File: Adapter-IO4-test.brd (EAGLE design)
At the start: 22 parts, among them CON1 CONNECTOR-IO4INV

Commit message: simplified design
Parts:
- removed LED5, LED6, LED7, LED8: (no value), SPCoast:LED5MM
- added BOARD1: BOARD50X50-NOHOLES, SPCoast:BOARD-SEEED5X5-NOHOLES
- moved Q1 36.9 mm to (5.71, 41.3), turned to 90 degrees
- moved Q2 36.9 mm to (15.9, 41.3), turned to 90 degrees
- moved Q3 36.9 mm to (26.0, 41.3), turned to 90 degrees
- moved Q4 36.9 mm to (36.2, 41.3), turned to 90 degrees
- moved LED1 29.2 mm to (10.8, 37.5)
- moved LED2 29.2 mm to (21.0, 37.5)
- moved LED3 29.2 mm to (31.1, 37.5)
- moved LED4 29.2 mm to (41.3, 37.5)
- moved R1 29.2 mm to (5.71, 37.5)
- moved R2 29.2 mm to (15.9, 37.5)
- moved R3 29.2 mm to (26.0, 37.5)
- moved R4 29.2 mm to (36.2, 37.5)
- moved SW1 5.24 mm to (10.8, 29.8)
- moved SW2 5.24 mm to (21.0, 29.8)
- moved SW3 5.24 mm to (31.1, 29.8)
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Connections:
- net GND: no longer LED5.K, LED6.K, LED7.K, LED8.K
- net N$16: no longer LED8.A
- net N$2: no longer LED5.A
- net N$4: no longer LED6.A
- net N$6: no longer LED7.A
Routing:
- net N$7: track 95.0 -> 70.2 mm
- net N$10: track 75.1 -> 59.5 mm
- net N$8: track 76.7 -> 63.1 mm, vias 3 -> 2
- net N$9: track 76.5 -> 63.4 mm, vias 3 -> 2
- net N$6: track 7.03 -> 3.13 mm
- net N$4: track 7.03 -> 3.13 mm
- net N$2: track 7.03 -> 3.13 mm
- net N$16: track 7.03 -> 3.13 mm
- net GND: track 15.6 -> 19.5 mm
- net VCC: track 94.2 -> 97.7 mm, vias 0 -> 2
- net N$1: track 3.05 -> 3.89 mm
- net N$15: track 3.08 -> 3.89 mm
- net N$5: track 3.08 -> 3.89 mm
- net N$3: track 3.08 -> 3.89 mm
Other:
- board outline added: 50 x 50 mm
- board text added: "2020-05"
- board text added: "v1.1"
- board text removed: "2020-01"
- board text removed: "v1.0"

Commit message: added values to schematic
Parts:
- LED1, LED2, LED3, LED4: value (none) -> Y
- R1, R2, R3, R4: value (none) -> 2k0
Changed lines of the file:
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@@
 <attribute name="VALUE" x="46.355" y="26.797" size="1.27" layer="27" ratio="10" rot="R90"/>
 </element>
-<element name="LED1" library="SPCoast" package="0805-LED" value="" x="10.795" y="37.465" smashed="yes">
+<element name="LED1" library="SPCoast" package="0805-LED" value="Y" x="10.795" y="37.465" smashed="yes">
 <attribute name="NAME" x="9.525" y="42.545" size="1.27" layer="25"/>
 <attribute name="VALUE" x="9.525" y="34.925" size="1.27" layer="27"/>
 </element>
-<element name="LED2" library="SPCoast" package="0805-LED" value="" x="20.955" y="37.465" smashed="yes">
+<element name="LED2" library="SPCoast" package="0805-LED" value="Y" x="20.955" y="37.465" smashed="yes">
 <attribute name="NAME" x="19.685" y="42.545" size="1.27" layer="25"/>
 <attribute name="VALUE" x="19.685" y="34.925" size="1.27" layer="27"/>
 </element>
-<element name="LED3" library="SPCoast" package="0805-LED" value="" x="31.115" y="37.465" smashed="yes">
+<element name="LED3" library="SPCoast" package="0805-LED" value="Y" x="31.115" y="37.465" smashed="yes">
 <attribute name="NAME" x="29.845" y="42.545" size="1.27" layer="25"/>
 <attribute name="VALUE" x="29.845" y="34.925" size="1.27" layer="27"/>
 </element>
-<element name="LED4" library="SPCoast" package="0805-LED" value="" x="41.275" y="37.465" smashed="yes">
+<element name="LED4" library="SPCoast" package="0805-LED" value="Y" x="41.275" y="37.465" smashed="yes">
 <attribute name="NAME" x="40.005" y="42.545" size="1.27" layer="25"/>
 <attribute name="VALUE" x="40.005" y="34.925" size="1.27" layer="27"/>
 </element>
-<element name="R1" library="SPCoast" package="0805-RES" value="" x="5.715" y="37.465" smashed="yes" rot="R180">
+<element name="R1" library="SPCoast" package="0805-RES" value="2k0" x="5.715" y="37.465" smashed="yes" rot="R180">
 <attribute name="VALUE" x="6.731" y="38.862" size="0.4064" layer="27" rot="R180"/>
 </element>
-<element name="R2" library="SPCoast" package="0805-RES" value="" x="15.875" y="37.465" smashed="yes" rot="R180">
+<element name="R2" library="SPCoast" package="0805-RES" value="2k0" x="15.875" y="37.465" smashed="yes" rot="R180">
 <attribute name="VALUE" x="16.891" y="38.862" size="0.4064" layer="27" rot="R180"/>
 </element>
-<element name="R3" library="SPCoast" package="0805-RES" value="" x="26.035" y="37.465" smashed="yes" rot="R180">
+<element name="R3" library="SPCoast" package="0805-RES" value="2k0" x="26.035" y="37.465" smashed="yes" rot="R180">
 <attribute name="VALUE" x="27.051" y="38.862" size="0.4064" layer="27" rot="R180"/>
 </element>
-<element name="R4" library="SPCoast" package="0805-RES" value="" x="36.195" y="37.465" smashed="yes" rot="R180">
+<element name="R4" library="SPCoast" package="0805-RES" value="2k0" x="36.195" y="37.465" smashed="yes" rot="R180">
 <attribute name="VALUE" x="37.211" y="38.862" size="0.4064" layer="27" rot="R180"/>
 </element>

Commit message: added values to schematic
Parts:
- Q1, Q2, Q3, Q4: value (none) -> P-FET
- SW1, SW2, SW3, SW4: value (none) -> SPST-MOM
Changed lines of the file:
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@@
 <attribute name="VALUE" x="48.387" y="8.89" size="1.27" layer="27" font="vector" rot="R90"/>
 </element>
-<element name="Q1" library="SPCoast" package="SOT23-3" value="" x="5.715" y="41.275" smashed="yes" rot="R90">
+<element name="Q1" library="SPCoast" package="SOT23-3" value="P-FET" x="5.715" y="41.275" smashed="yes" rot="R90">
 <attribute name="VALUE" x="5.9055" y="40.259" size="0.4064" layer="27" rot="R90"/>
 </element>
-<element name="Q2" library="SPCoast" package="SOT23-3" value="" x="15.875" y="41.275" smashed="yes" rot="R90">
+<element name="Q2" library="SPCoast" package="SOT23-3" value="P-FET" x="15.875" y="41.275" smashed="yes" rot="R90">
 <attribute name="VALUE" x="16.0655" y="40.259" size="0.4064" layer="27" rot="R90"/>
 </element>
-<element name="Q3" library="SPCoast" package="SOT23-3" value="" x="26.035" y="41.275" smashed="yes" rot="R90">
+<element name="Q3" library="SPCoast" package="SOT23-3" value="P-FET" x="26.035" y="41.275" smashed="yes" rot="R90">
 <attribute name="VALUE" x="26.2255" y="40.259" size="0.4064" layer="27" rot="R90"/>
 </element>
-<element name="Q4" library="SPCoast" package="SOT23-3" value="" x="36.195" y="41.275" smashed="yes" rot="R90">
+<element name="Q4" library="SPCoast" package="SOT23-3" value="P-FET" x="36.195" y="41.275" smashed="yes" rot="R90">
 <attribute name="VALUE" x="36.3855" y="40.259" size="0.4064" layer="27" rot="R90"/>
 </element>
-<element name="SW1" library="SPCoast" package="B3F-10XX" value="" x="10.795" y="29.845" smashed="yes" rot="R90">
+<element name="SW1" library="SPCoast" package="B3F-10XX" value="SPST-MOM" x="10.795" y="29.845" smashed="yes" rot="R90">
 <attribute name="NAME" x="7.112" y="26.797" size="1.27" layer="25" ratio="10" rot="R90"/>
 <attribute name="VALUE" x="15.875" y="26.797" size="1.27" layer="27" ratio="10" rot="R90"/>
 </element>
-<element name="SW2" library="SPCoast" package="B3F-10XX" value="" x="20.955" y="29.845" smashed="yes" rot="R90">
+<element name="SW2" library="SPCoast" package="B3F-10XX" value="SPST-MOM" x="20.955" y="29.845" smashed="yes" rot="R90">
 <attribute name="NAME" x="17.272" y="26.797" size="1.27" layer="25" ratio="10" rot="R90"/>
 <attribute name="VALUE" x="26.035" y="26.797" size="1.27" layer="27" ratio="10" rot="R90"/>
 </element>
-<element name="SW3" library="SPCoast" package="B3F-10XX" value="" x="31.115" y="29.845" smashed="yes" rot="R90">
+<element name="SW3" library="SPCoast" package="B3F-10XX" value="SPST-MOM" x="31.115" y="29.845" smashed="yes" rot="R90">
 <attribute name="NAME" x="27.432" y="26.797" size="1.27" layer="25" ratio="10" rot="R90"/>
 <attribute name="VALUE" x="36.195" y="26.797" size="1.27" layer="27" ratio="10" rot="R90"/>
 </element>
-<element name="SW4" library="SPCoast" package="B3F-10XX" value="" x="41.275" y="29.845" smashed="yes" rot="R90">
+<element name="SW4" library="SPCoast" package="B3F-10XX" value="SPST-MOM" x="41.275" y="29.845" smashed="yes" rot="R90">
 <attribute name="NAME" x="37.592" y="26.797" size="1.27" layer="25" ratio="10" rot="R90"/>
 <attribute name="VALUE" x="46.355" y="26.797" size="1.27" layer="27" ratio="10" rot="R90"/>

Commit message: added value G to LEDs
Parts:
- LED1, LED2, LED3, LED4: value Y -> G
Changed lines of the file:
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@@
 <attribute name="VALUE" x="46.355" y="26.797" size="1.27" layer="27" ratio="10" rot="R90"/>
 </element>
-<element name="LED1" library="SPCoast" package="0805-LED" value="Y" x="10.795" y="37.465" smashed="yes">
+<element name="LED1" library="SPCoast" package="0805-LED" value="G" x="10.795" y="37.465" smashed="yes">
 <attribute name="NAME" x="9.525" y="42.545" size="1.27" layer="25"/>
 <attribute name="VALUE" x="9.525" y="34.925" size="1.27" layer="27"/>
 </element>
-<element name="LED2" library="SPCoast" package="0805-LED" value="Y" x="20.955" y="37.465" smashed="yes">
+<element name="LED2" library="SPCoast" package="0805-LED" value="G" x="20.955" y="37.465" smashed="yes">
 <attribute name="NAME" x="19.685" y="42.545" size="1.27" layer="25"/>
 <attribute name="VALUE" x="19.685" y="34.925" size="1.27" layer="27"/>
 </element>
-<element name="LED3" library="SPCoast" package="0805-LED" value="Y" x="31.115" y="37.465" smashed="yes">
+<element name="LED3" library="SPCoast" package="0805-LED" value="G" x="31.115" y="37.465" smashed="yes">
 <attribute name="NAME" x="29.845" y="42.545" size="1.27" layer="25"/>
 <attribute name="VALUE" x="29.845" y="34.925" size="1.27" layer="27"/>
 </element>
-<element name="LED4" library="SPCoast" package="0805-LED" value="Y" x="41.275" y="37.465" smashed="yes">
+<element name="LED4" library="SPCoast" package="0805-LED" value="G" x="41.275" y="37.465" smashed="yes">
 <attribute name="NAME" x="40.005" y="42.545" size="1.27" layer="25"/>
 <attribute name="VALUE" x="40.005" y="34.925" size="1.27" layer="27"/>

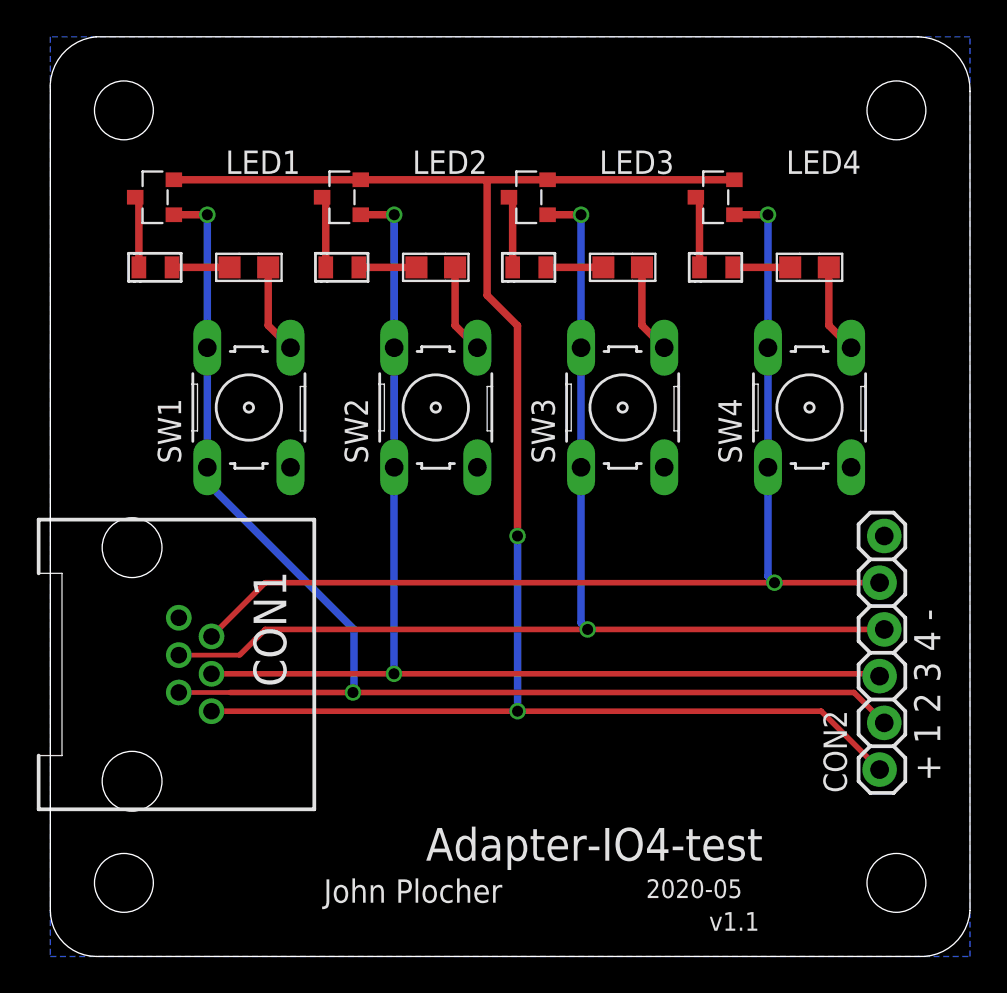
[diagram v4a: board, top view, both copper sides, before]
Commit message: fixed SPCoast lbr part orientation
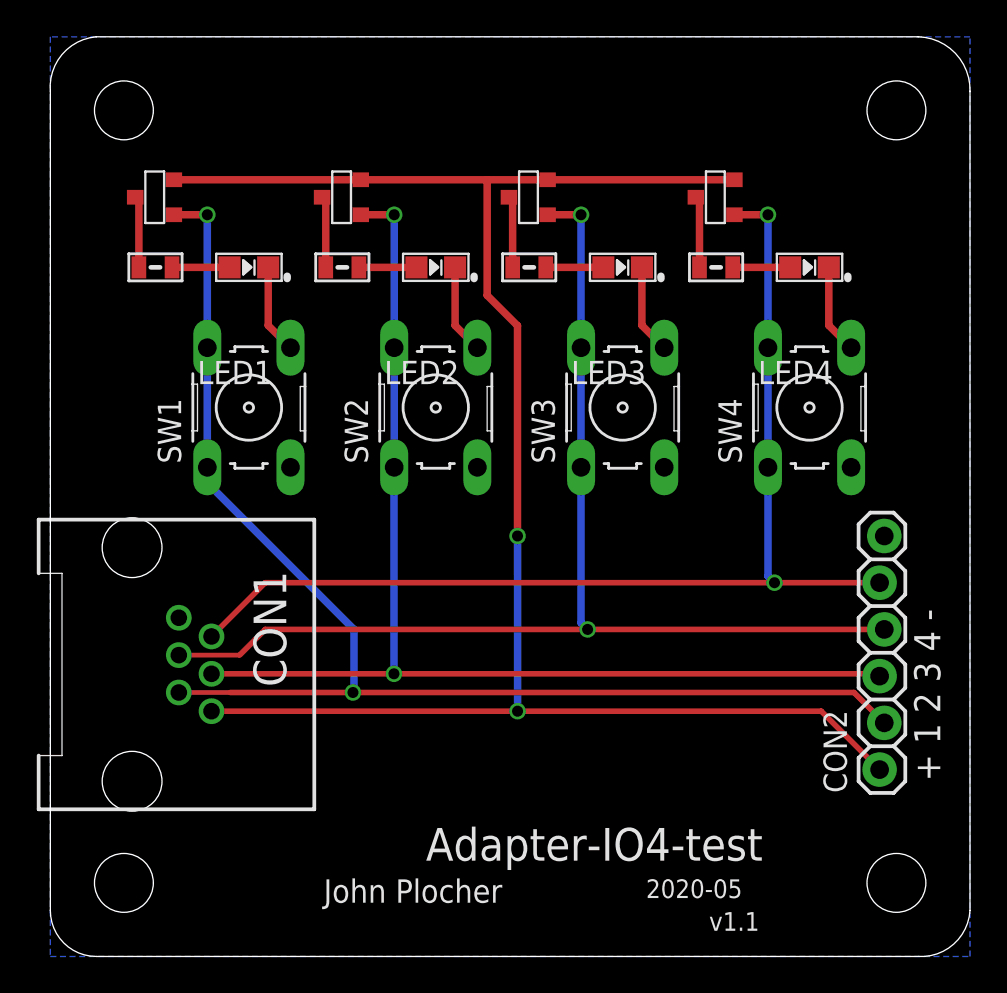
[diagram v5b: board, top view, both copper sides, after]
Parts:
- CON1: value CONNECTOR-IO4INV -> (none)
- turned LED1 to 180 degrees
- turned LED2 to 180 degrees
- turned LED3 to 180 degrees
- turned LED4 to 180 degrees
- turned Q1 to 0 degrees
- turned Q2 to 0 degrees
- turned Q3 to 0 degrees
- turned Q4 to 0 degrees

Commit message: added values for connectors
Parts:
- CON1: value (none) -> RJ12/6
- CON2: value (none) -> 0.100
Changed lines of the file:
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@@
 </autorouter>
 <elements>
-<element name="CON1" library="SPCoast" package="RJ25-INVERTED" value="" x="4.445" y="15.875" smashed="yes" rot="R270">
+<element name="CON1" library="SPCoast" package="RJ25-INVERTED" value="RJ12/6" x="4.445" y="15.875" smashed="yes" rot="R270">
 <attribute name="NAME" x="11.049" y="20.955" size="1.778" layer="25" rot="R270"/>
 </element>
-<element name="CON2" library="SPCoast" package="1X06_LOCK" value="" x="45.085" y="10.16" smashed="yes" rot="R90">
+<element name="CON2" library="SPCoast" package="1X06_LOCK" value="0.100" x="45.085" y="10.16" smashed="yes" rot="R90">
 <attribute name="NAME" x="43.307" y="8.89" size="1.27" layer="25" font="vector" rot="R90"/>
 <attribute name="VALUE" x="48.387" y="8.89" size="1.27" layer="27" font="vector" rot="R90"/>
